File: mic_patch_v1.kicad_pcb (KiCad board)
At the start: 4 copper layers, 40 x 31 mm, 55 parts, among them J1 Conn_ARM_SWD_TagConnect_TC203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, J2 J_000002, J3 J_000001, J4 Micro_SD_Card, J5 J_000003, P0.24 GPIO Breakout P0.24, P1.06 GPIO Breakout P1.06, SW1 SW_000001, SW2 SW_000001, U1 NORA-B106-00B, U2 PWR_nPM1100-QDXX, U3 ADAU7002ACBZ-R7, Y1 CLK_0003

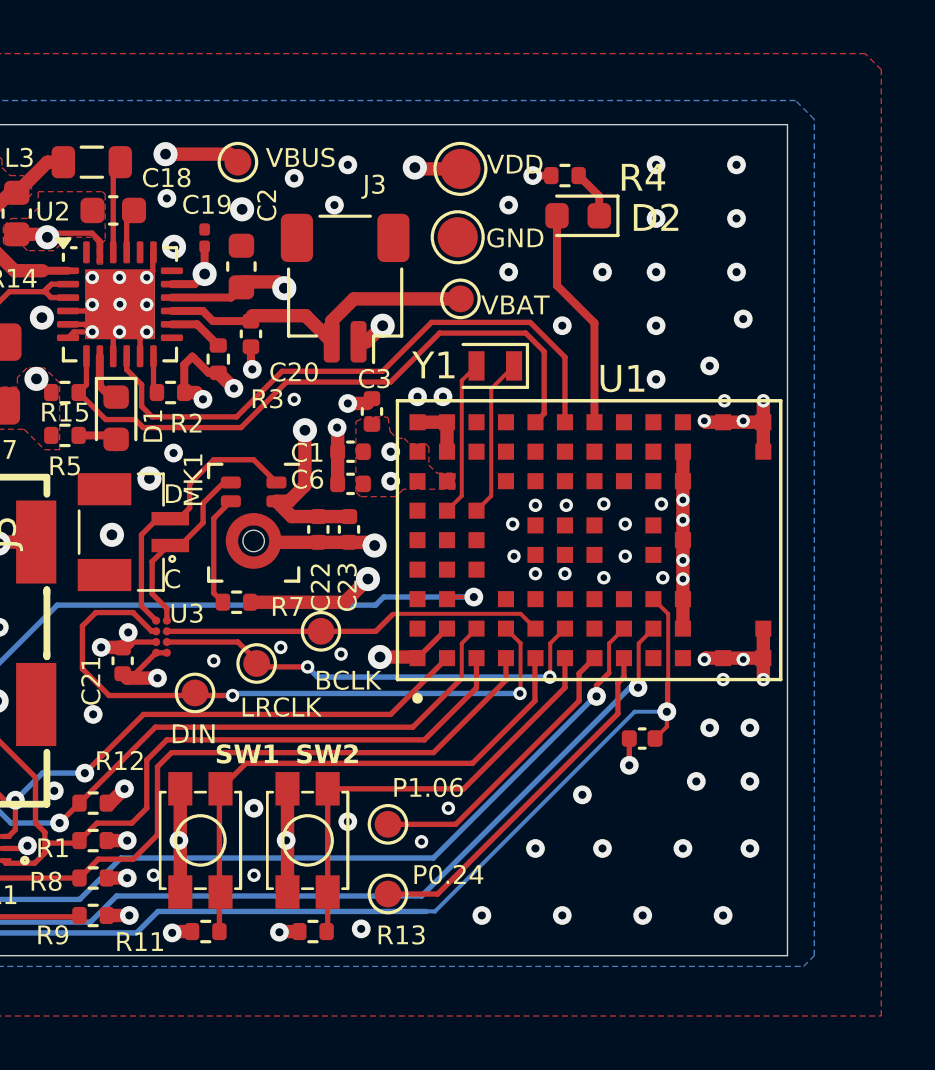
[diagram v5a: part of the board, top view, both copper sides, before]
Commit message: corrected missing part numbers + inconsistencies
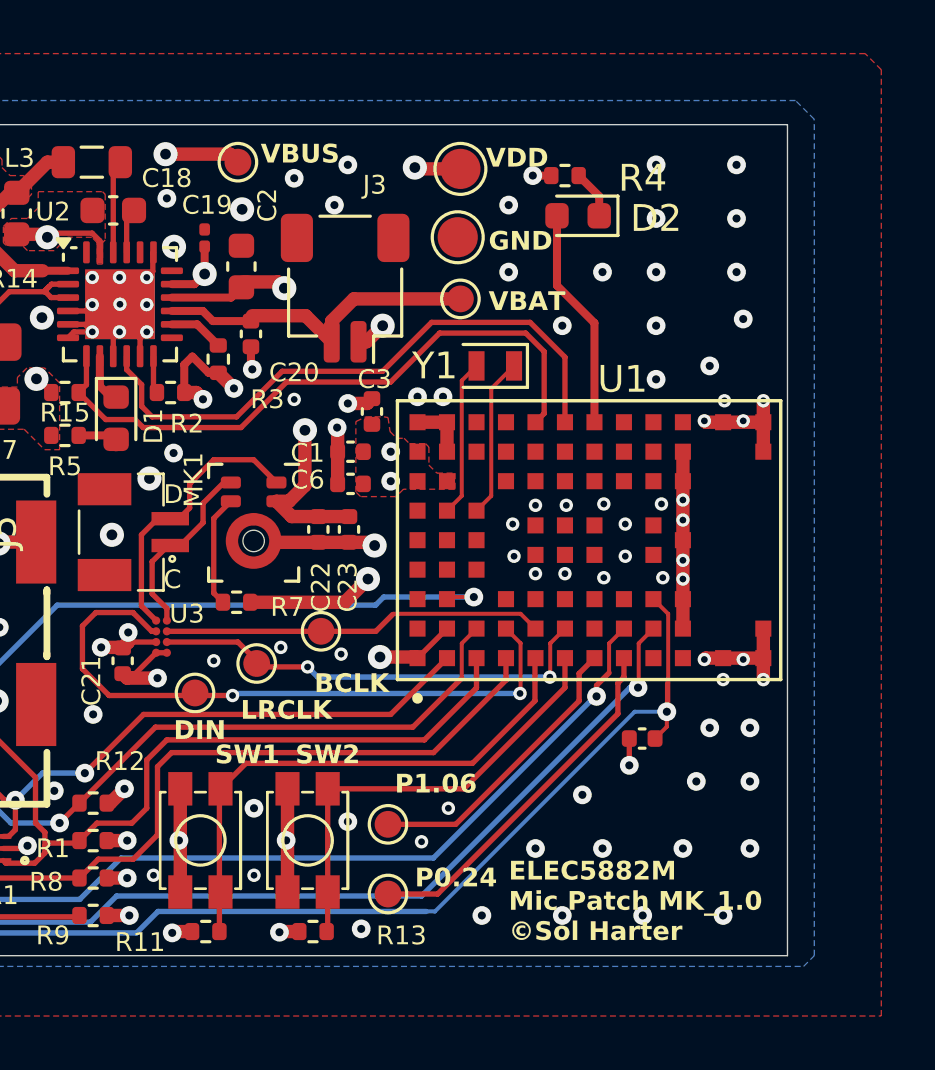
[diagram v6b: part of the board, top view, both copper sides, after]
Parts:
- R1, R10, R11, R12, R13, R15, R3, R7, R8, R9: value R_00002 -> R_00003
- renumbered VDD to TP1, GND to TP2, VBAT to TP3, VBUS to TP4, P1.06 to TP5, P0.24 to TP6, LRCLK to TP7, BCLK to TP8, DIN to TP9
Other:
- board text added: "BCLK"
- board text added: "DIN"
- board text added: "ELEC5882M Mic Patch MK_1.0 ©Sol Harter"
- board text added: "GND"
- board text added: "LRCLK"
- board text added: "P0.24"
- board text added: "P1.06"
- board text added: "VBAT"
- board text added: "VBUS"
- board text added: "VDD"
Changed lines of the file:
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@@
 		(descr "SMD pad as test Point, diameter 1.5mm")
 		(tags "test point SMD pad")
-		(property "Reference" "VDD"
+		(property "Reference" "TP1"
 			(at 2.05 -0.15 0)
 			(layer "F.SilkS")
+			(hide yes)
 			(effects
 				(font
@@
 			)
 		)
-		(property "Value" "R_00002"
+		(property "Value" "R_00003"
 			(at 0 1.17 -90)
 			(layer "F.Fab")
@@
 		(descr "SMD pad as test Point, diameter 1.0mm")
 		(tags "test point SMD pad")
-		(property "Reference" "P0.24"
+		(property "Reference" "TP6"
 			(at 2.25 -0.7 0)
 			(layer "F.SilkS")
+			(hide yes)
 			(effects
 				(font
@@
 			)
 		)
-		(property "Value" "R_00002"
+		(property "Value" "R_00003"
 			(at 0 1.17 0)
 			(layer "F.Fab")
@@
 		(descr "SMD pad as test Point, diameter 1.0mm")
 		(tags "test point SMD pad")
-		(property "Reference" "BCLK"
+		(property "Reference" "TP8"
 			(at 1 1.85 0)
 			(layer "F.SilkS")
+			(hide yes)
 			(effects
 				(font
@@
 			)
 		)
-		(property "Value" "R_00002"
+		(property "Value" "R_00003"
 			(at 0 1.17 180)
 			(layer "F.Fab")
@@
 		(tags "capacitor")
 		(property "Reference" "C22"
-			(at -2.15 0.1 270)
+			(at -2.15 0.1 -90)
 			(layer "F.SilkS")
 			(effects
@@
 		(descr "SMD pad as test Point, diameter 1.0mm")
 		(tags "test point SMD pad")
-		(property "Reference" "LRCLK"
+		(property "Reference" "TP7"
 			(at 0.9 1.65 0)
 			(layer "F.SilkS")
+			(hide yes)
 			(effects
 				(font
@@
 			)
 		)
-		(property "Value" "R_00002"
+		(property "Value" "R_00003"
 			(at 0 1.17 180)
 			(layer "F.Fab")
@@
 			)
 		)
-		(property "Value" "R_00002"
+		(property "Value" "R_00003"
 			(at 0 1.17 180)
 			(layer "F.Fab")
@@
 			)
 		)
-		(property "Value" "R_00002"
+		(property "Value" "R_00003"
 			(at 0 1.17 0)
 			(layer "F.Fab")
@@
 		(descr "SMD pad as test Point, diameter 1.5mm")
 		(tags "test point SMD pad")
-		(property "Reference" "GND"
+		(property "Reference" "TP2"
 			(at 2.15 0.05 0)
 			(layer "F.SilkS")
+			(hide yes)
 			(effects
 				(font
@@
 			)
 		)
-		(property "Value" "R_00002"
+		(property "Value" "R_00003"
 			(at 0 1.17 0)
 			(layer "F.Fab")
@@
 			)
 		)
-		(property "Value" "R_00002"
+		(property "Value" "R_00003"
 			(at 0 1.17 180)
 			(layer "F.Fab")
@@
 			)
 		)
-		(property "Value" "R_00002"
+		(property "Value" "R_00003"
 			(at 0 1.17 180)
 			(layer "F.Fab")
@@
 			)
 		)
-		(property "LCSC PNs" ""
+		(property "LCSC PNs" "C17477"
 			(at 0 0 180)
 			(unlocked yes)
@@
 		(descr "SMD pad as test Point, diameter 1.0mm")
 		(tags "test point SMD pad")
-		(property "Reference" "VBUS"
+		(property "Reference" "TP4"
 			(at 2.35 -0.15 0)
 			(layer "F.SilkS")
+			(hide yes)
 			(effects
 				(font
@@
 		(descr "SMD pad as test Point, diameter 1.0mm")
 		(tags "test point SMD pad")
-		(property "Reference" "DIN"
+		(property "Reference" "TP9"
 			(at -0.05 1.55 0)
 			(layer "F.SilkS")
+			(hide yes)
 			(effects
 				(font
@@
 		(tags "capacitor")
 		(property "Reference" "C2"
-			(at 2.2926 0.9694 270)
+			(at 2.2926 0.9694 -90)
 			(layer "F.SilkS")
 			(effects
@@
 			)
 		)
-		(property "Value" "R_00002"
+		(property "Value" "R_00003"
 			(at 0 1.17 0)
 			(layer "F.Fab")
@@
 		(tags "capacitor")
 		(property "Reference" "C21"
-			(at -0.75 -1.16 270)
+			(at -0.75 -1.16 -90)
 			(layer "F.SilkS")
 			(effects
@@
 			)
 		)
+		(property "LCSC PNs" "C7249860"
+			(at 0 0 0)
+			(unlocked yes)
+			(layer "F.Fab")
+			(hide yes)
+			(effects
+				(font
+					(size 1 1)
+					(thickness 0.15)
+				)
+			)
+		)
 		(property ki_fp_filters "QFN*1EP*4x4mm*P0.5mm*EP2.6x2.6mm*")
 		(sheetname "Power")
@@
 			)
 		)
+		(property "LC" ""
+			(at 0 0 180)
+			(unlocked yes)
+			(layer "F.Fab")
+			(hide yes)
+			(effects
+				(font
+					(size 1 1)
+					(thickness 0.15)
+				)
+			)
+		)
+		(property "LCSC PNs" "C552534"
+			(at 0 0 180)
+			(unlocked yes)
+			(layer "F.Fab")
+			(hide yes)
+			(effects
+				(font
+					(size 1 1)
+					(thickness 0.15)
+				)
+			)
+		)
 		(property ki_fp_filters "DFN1308-6_SOT8006_NEX DFN1308-6_SOT8006_NEX-M DFN1308-6_SOT8006_NEX-L")
 		(sheetname "SD_card")
@@
 		(tags "capacitor")
 		(property "Reference" "C23"
-			(at -2.15 -0.043 270)
+			(at -2.15 -0.043 -90)
 			(layer "F.SilkS")
 			(effects
@@
 		(descr "SMD pad as test Point, diameter 1.0mm")
 		(tags "test point SMD pad")
-		(property "Reference" "P1.06"
+		(property "Reference" "TP5"
 			(at 1.5 -1.35 0)
 			(layer "F.SilkS")
+			(hide yes)
 			(effects
 				(font
@@
 		(descr "SMD pad as test Point, diameter 1.0mm")
 		(tags "test point SMD pad")
-		(property "Reference" "VBAT"
+		(property "Reference" "TP3"
 			(at 2.05 0.25 0)
 			(layer "F.SilkS")
+			(hide yes)
 			(effects
 				(font
@@
 		(layer "Edge.Cuts")
 	)
+	(gr_text "ELEC5882M\nMic Patch MK_1.0\n©Sol Harter"
+		(at 159.5 120 0)
+		(layer "F.SilkS")
+		(effects
+			(font
+				(size 0.7 0.7)
+				(thickness 0.15)
+				(bold yes)
+			)
+			(justify left bottom)
+		)
+	)
+	(gr_text "P0.24"
+		(at 156 118 0)
+		(layer "F.SilkS")
+		(effects
+			(font
+				(size 0.7 0.7)
+				(thickness 0.15)
+				(bold yes)
+			)
+			(justify left bottom)
+		)
+	)
 	(gr_text "C"
 		(at 146.625 106.875 0)
@@
 		)
 	)
+	(gr_text "P1.06"
+		(at 155.25 114.5 0)
+		(layer "F.SilkS")
+		(effects
+			(font
+				(size 0.7 0.7)
+				(thickness 0.15)
+				(bold yes)
+			)
+			(justify left bottom)
+		)
+	)
+	(gr_text "VDD"
+		(at 158.65 91.15 0)
+		(layer "F.SilkS")
+		(effects
+			(font
+				(size 0.7 0.7)
+				(thickness 0.15)
+				(bold yes)
+			)
+			(justify left bottom)
+		)
+	)
+	(gr_text "VBUS"
+		(at 150.25 91 0)
+		(layer "F.SilkS")
+		(effects
+			(font
+				(size 0.7 0.7)
+				(thickness 0.15)
+				(bold yes)
+			)
+			(justify left bottom)
+		)
+	)
+	(gr_text "GND"
+		(at 158.75 94.25 0)
+		(layer "F.SilkS")
+		(effects
+			(font
+				(size 0.7 0.7)
+				(thickness 0.15)
+				(bold yes)
+			)
+			(justify left bottom)
+		)
+	)
+	(gr_text "DIN"
+		(at 147 112.5 0)
+		(layer "F.SilkS")
+		(effects
+			(font
+				(size 0.7 0.7)
+				(thickness 0.15)
+				(bold yes)
+			)
+			(justify left bottom)
+		)
+	)
+	(gr_text "LRCLK"
+		(at 149.5 111.75 0)
+		(layer "F.SilkS")
+		(effects
+			(font
+				(size 0.7 0.7)
+				(thickness 0.15)
+				(bold yes)
+			)
+			(justify left bottom)
+		)
+	)
+	(gr_text "BCLK"
+		(at 152.25 110.75 0)
+		(layer "F.SilkS")
+		(effects
+			(font
+				(size 0.7 0.7)
+				(thickness 0.15)
+				(bold yes)
+			)
+			(justify left bottom)
+		)
+	)
 	(gr_text "D"
 		(at 146.625 103.7 0)
@@
 			)
 			(justify left bottom)
+		)
+	)
+	(gr_text "VBAT\n"
+		(at 158.75 96.5 0)
+		(layer "F.SilkS")
+		(effects
+			(font
+				(size 0.7 0.7)
+				(thickness 0.15)
+				(bold yes)
+			)
+			(justify left bottom)

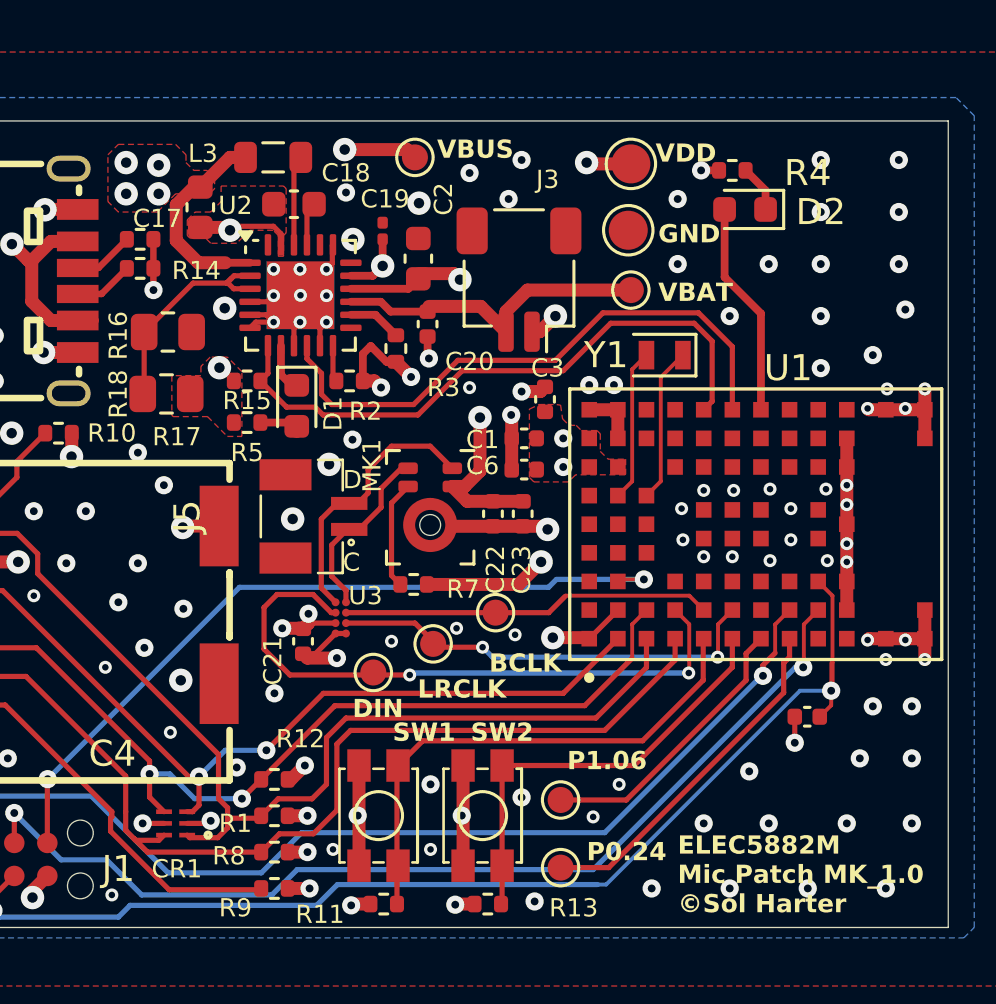
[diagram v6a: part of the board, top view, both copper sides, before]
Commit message: updated ESD footprint
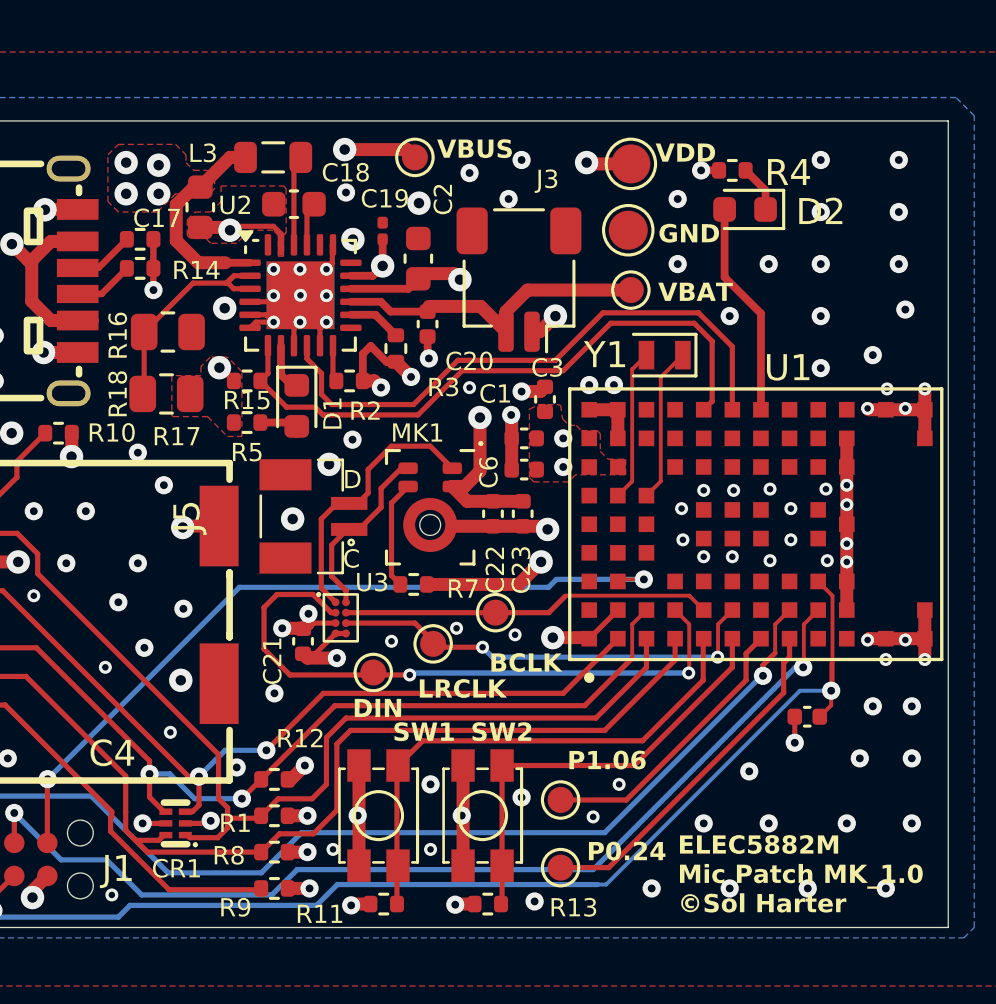
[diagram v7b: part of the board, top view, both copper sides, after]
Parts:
- CR1: footprint mic_patch_parts:DFN1308-6_SOT8006_NEX -> mic_patch_parts:SOT8006_C552534
- turned CR1 to 90 degrees
